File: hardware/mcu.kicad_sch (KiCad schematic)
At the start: 4 parts, among them U6 T113-S3

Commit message: 主晶片頁 C17~C19 footprint 由 DIP-24 改為 C_0603_1608Metric
複製元件時帶過去的錯誤封裝,check_power_rails.py 的 footprint 檢查抓到。
0.1uF ×2、2.2uF ×1 皆照 012 §4.1 用 0603。

Co-Authored-By: Claude Opus 5.5 <noreply@anthropic.com>
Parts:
- C17, C18, C19: footprint Package_DIP:DIP-24_W7.62mm -> Capacitor_SMD:C_0603_1608Metric
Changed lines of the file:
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@@
 			)
 		)
-		(property "Footprint" "Package_DIP:DIP-24_W7.62mm"
+		(property "Footprint" "Capacitor_SMD:C_0603_1608Metric"
 			(at 311.15 135.5852 0)
 			(hide yes)
@@
 			)
 		)
-		(property "Footprint" "Package_DIP:DIP-24_W7.62mm"
+		(property "Footprint" "Capacitor_SMD:C_0603_1608Metric"
 			(at 295.91 138.1252 0)
 			(hide yes)
@@
 			)
 		)
-		(property "Footprint" "Package_DIP:DIP-24_W7.62mm"
+		(property "Footprint" "Capacitor_SMD:C_0603_1608Metric"
 			(at 311.15 120.3452 0)
 			(hide yes)

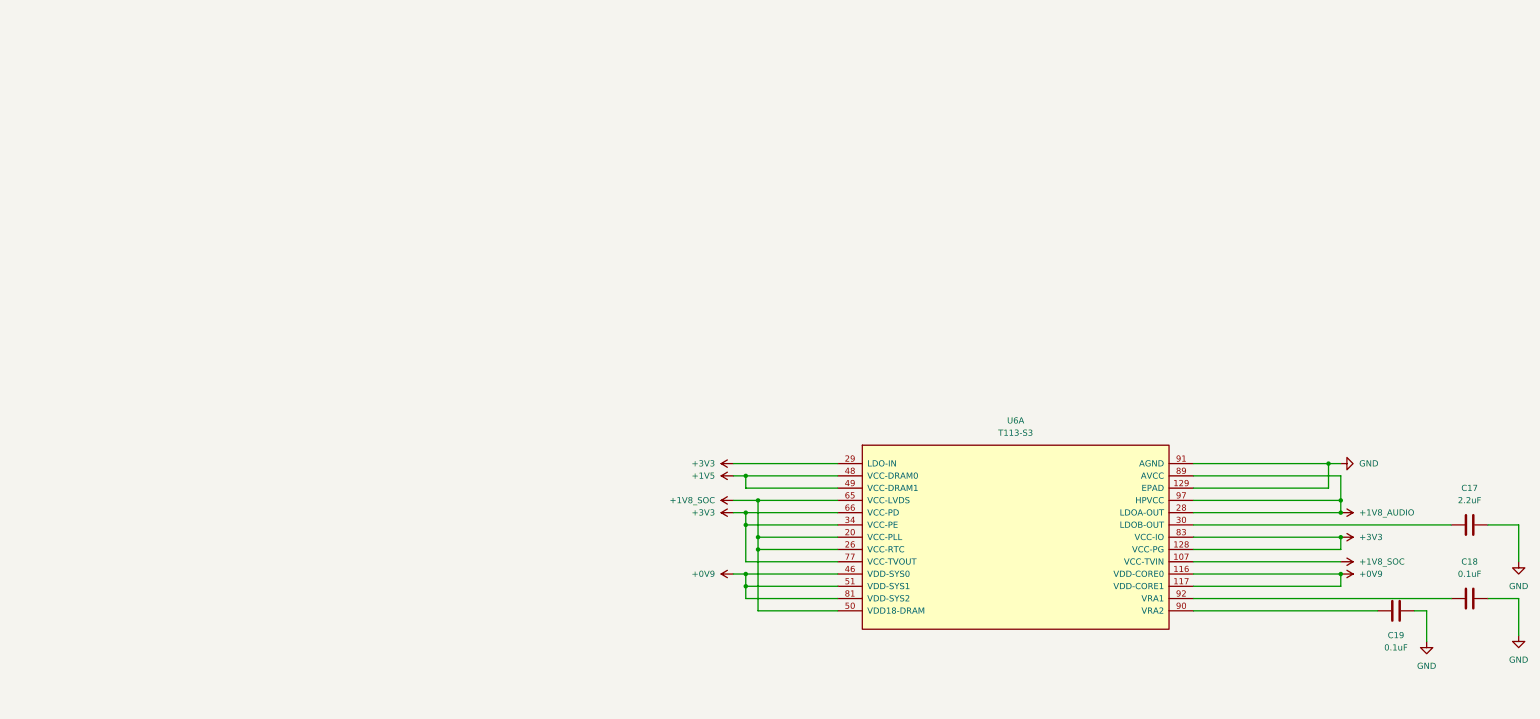
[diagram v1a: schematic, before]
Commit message: unit 2 的 12 腳接上全域標籤;修回被 KiCad 覆蓋的 footprint
unit 2（PB/PC/PF）先接 microSD 與 SPI NOR 這 12 腳:
  PF0~PF5 → SDC0_D1/D0/CLK/CMD/D3/D2
  PC2~PC7 → SPI0_CLK/CS0/MOSI/MISO/WP/HOLD
SDC0 的資料線編號不順(PF0=D1、PF1=D0、PF4=D3、PF5=D2),照 DS 抄,已核對無誤。
PF6 與 PB2~PB7 本輪不接。

★ C17~C19 的 footprint 被 KiCad 洗回 DIP-24:
  2413442 已經改成 C_0603 並 commit,但 KiCad 還開著舊的記憶體狀態,
  畫完 unit 2 存檔時整頁寫回去,把修正覆蓋掉。
  危險在於 git 只顯示「檔案被修改」,看不出是哪些修正被洗掉。
  → 012 新增 §6.2:git pull 之後、或任何人在檔案層改過 .kicad_sch 之後,
    一律關掉 KiCad 再重開。

check_power_rails.py 的跨頁白名單擴充 SDC0_* 與 SPI0_* 共 12 條,
附等待對象(儲存頁的 microSD 座 / SPI NOR)。

Co-Authored-By: Claude Opus 5 <noreply@anthropic.com>
Claude-Session: https://claude.ai/code/session_01HtGUWSQFey6W2g2grqgTMR
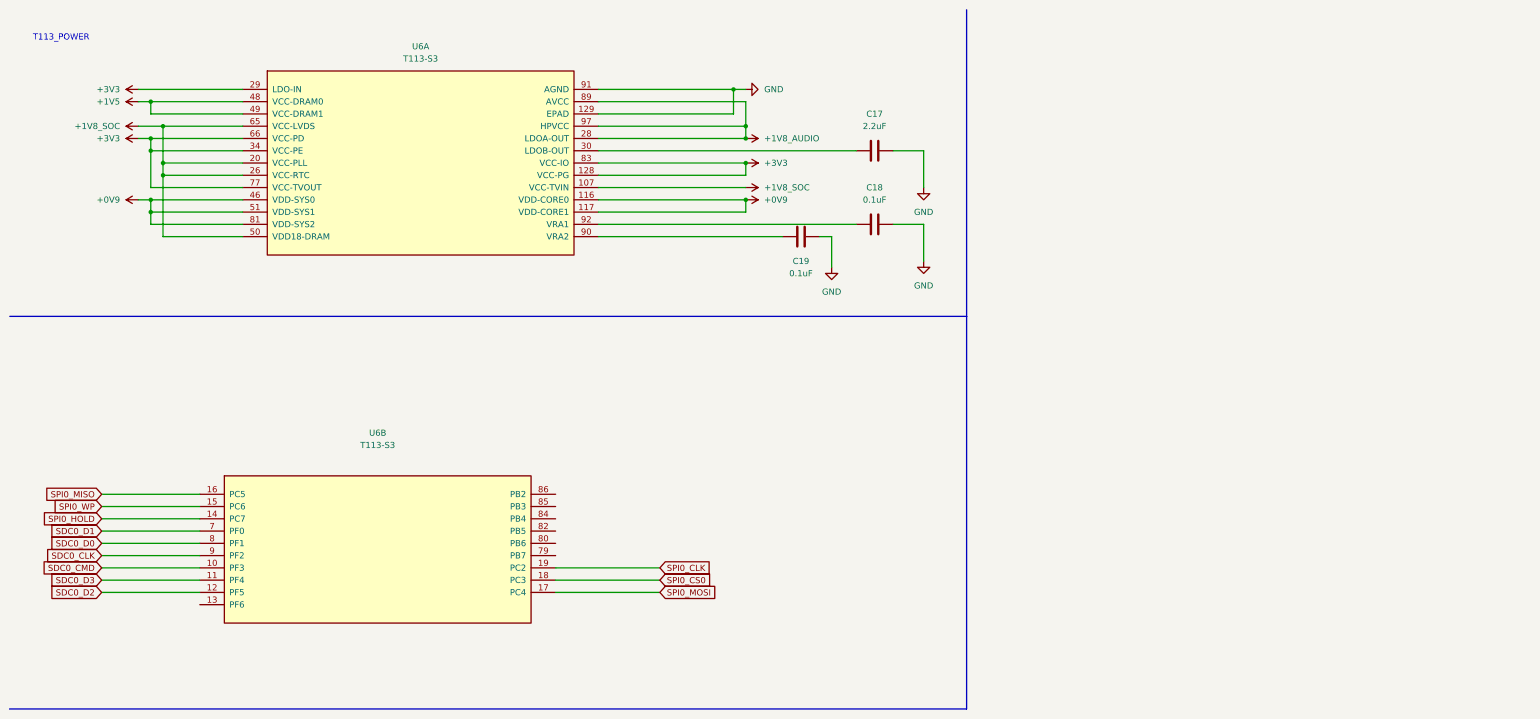
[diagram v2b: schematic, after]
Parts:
- added unit 2 of U6
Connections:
- new net SDC0_CLK: U6.9 (PF2)
- new net SDC0_CMD: U6.10 (PF3)
- new net SDC0_D0: U6.8 (PF1)
- new net SDC0_D1: U6.7 (PF0)
- new net SDC0_D2: U6.12 (PF5)
- new net SDC0_D3: U6.11 (PF4)
- new net SPI0_CLK: U6.19 (PC2)
- new net SPI0_CS0: U6.18 (PC3)
- new net SPI0_HOLD: U6.14 (PC7)
- new net SPI0_MISO: U6.16 (PC5)
- new net SPI0_MOSI: U6.17 (PC4)
- new net SPI0_WP: U6.15 (PC6)
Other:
- note added: "T113_POWER"
- moved on the sheet: C17, C18, C19, U6A

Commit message: ★ unit 2 完成(19/19):PB2~PB7 與 PF6 改為測試點
去處:
  SDC0 → microSD   PF0~PF5   全域標籤
  SPI0 → SPI NOR   PC2~PC7   全域標籤
  測試點            PB2~PB7   TP1~TP6
                   PF6       TP7
  皆用 TestPoint:TestPoint_Pad_D1.5mm,BOM 成本 $0(只是裸銅焊盤)

★ 推翻 007 §6.3 原本的「PB2~PB7 = I2S2 音訊 codec」規劃:
  查 Table 4-3 發現 I2S2 的 mux 有兩組(PB2~PB7 與 PF0/1/3/5/6),
  PF 那組已給 SDC0;但本板音訊是 T113 內建 codec(unit 6 的 AVCC/HPVCC/HPOUTL-R),
  根本不需要外接 I2S codec → 這 6 腳沒有用途。
  不拉排針的理由是 §4 規則①:PB 在 VCC-IO bank,
  那條軌掛著 microSD + SPI NOR + UART0 console,燒了就變無法診斷的磚。

⚠ SDC0 資料線編號不順(PF0=D1、PF1=D0、PF4=D3、PF5=D2),照 DS 抄已核對。

check_power_rails.py 跨頁白名單已含 SDC0_*/SPI0_* 共 12 條。

Co-Authored-By: Claude Opus 5 <noreply@anthropic.com>
Claude-Session: https://claude.ai/code/session_01HtGUWSQFey6W2g2grqgTMR
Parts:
- added TP1, TP2, TP3, TP4, TP5, TP6, TP7: TestPoint, TestPoint:TestPoint_Pad_D1.5mm, symbol Connector:TestPoint
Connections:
- net at U6.13 (PF6): now also TP7.1
- net at U6.79 (PB7): now also TP6.1
- net at U6.80 (PB6): now also TP5.1
- net at U6.82 (PB5): now also TP4.1
- net at U6.84 (PB4): now also TP3.1
- net at U6.85 (PB3): now also TP2.1
- net at U6.86 (PB2): now also TP1.1

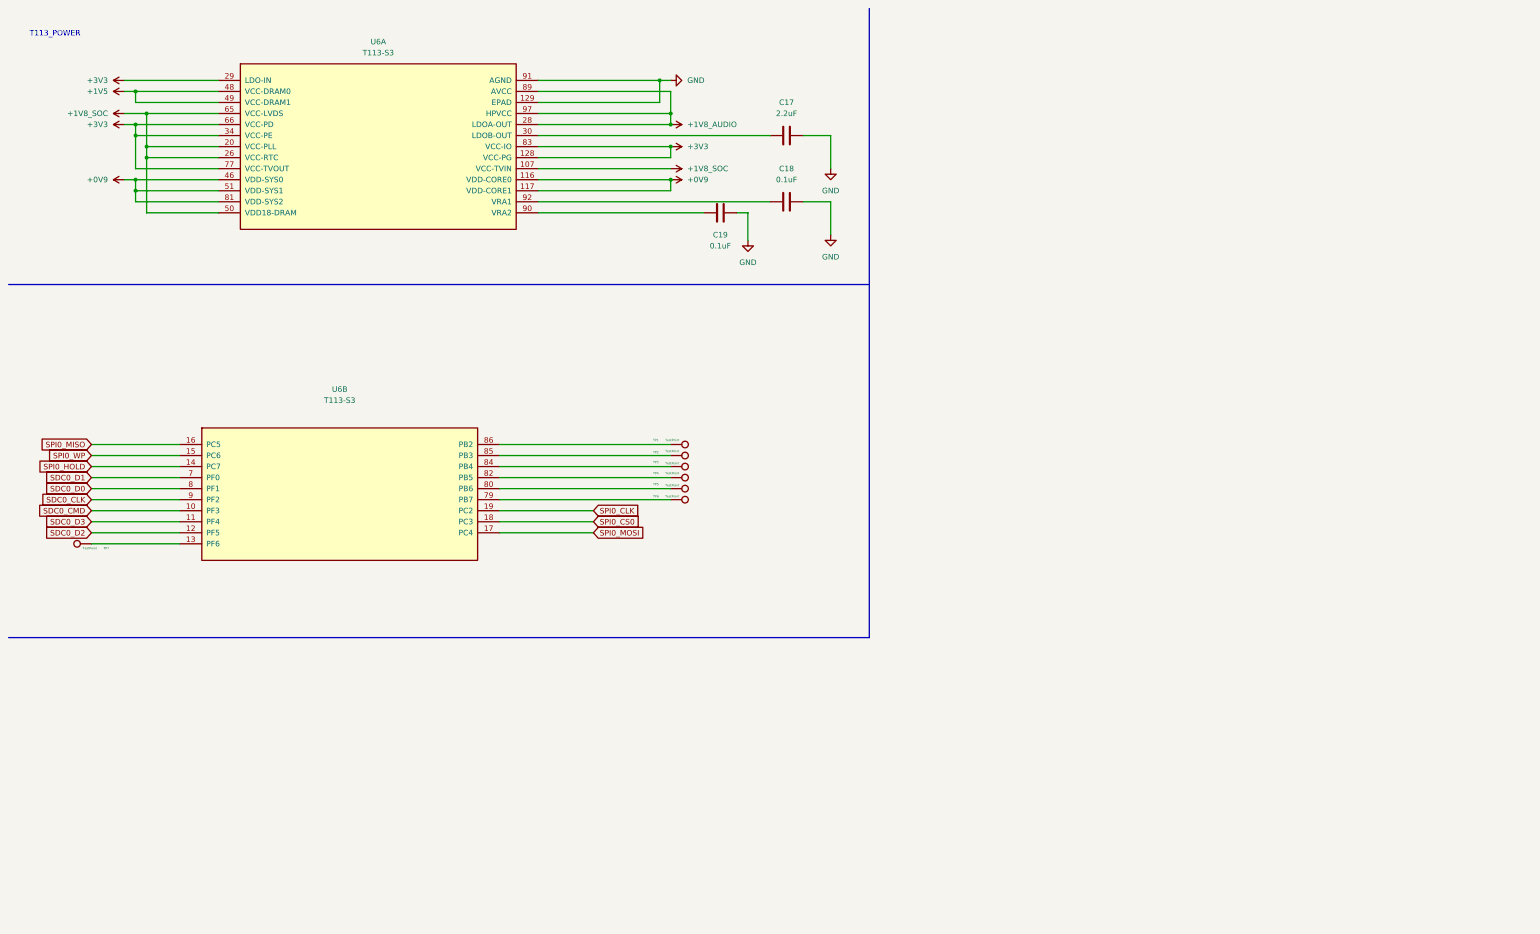
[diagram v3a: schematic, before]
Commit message: ★ unit 3 完成(23/23):MIPI 直通 + 0Ω 分支到 RGB
PD0~PD9    一分為二:MIPI 標籤直通、再經 R10~R19(0R) 分支到 RGB 標籤
PD10~PD21  直接接 LCD0_D14/D15/D18~D23/CLK/DE/HSYNC/VSYNC
PD22       測試點 TP8

0Ω 不在 MIPI 路徑上而在分支上,所以不違反「MIPI 不能加串聯電阻」。
跑 MIPI 時 0Ω 不焊,ADV7511 完全脫離主幹(概念 ⑤)。

三個照 DS 抄、不能推的地方(已逐行對 Table 4-3 核):
  LCD0-D 跳號①  PD5=D7 → PD6=D10
  LCD0-D 跳號②  PD11=D15 → PD12=D18(D16/D17 在 PB6/PB7,已放棄 → RGB666 的由來)
  pin 號順序反   PD12=pin70、PD13=pin69
這種地方推錯了 netlist 也看不出來 —— 名字都是合法的 LCD0_Dxx。

check_power_rails.py 跨頁白名單補 DSI_* 10 條 + LCD0_* 22 條。
R10~R19 與 TP8 的 footprint 一併填上。

★ 自我檢討:012 §6.2 剛寫完「KiCad 開著時不要在檔案層改 .kicad_sch」,
下一個動作就違反了 —— 偵測到 KiCad 開著只印了警告就繼續執行。
教訓:警告訊息不是防護措施,要擋就要硬性中止。

Co-Authored-By: Claude Opus 5 <noreply@anthropic.com>
Claude-Session: https://claude.ai/code/session_01HtGUWSQFey6W2g2grqgTMR
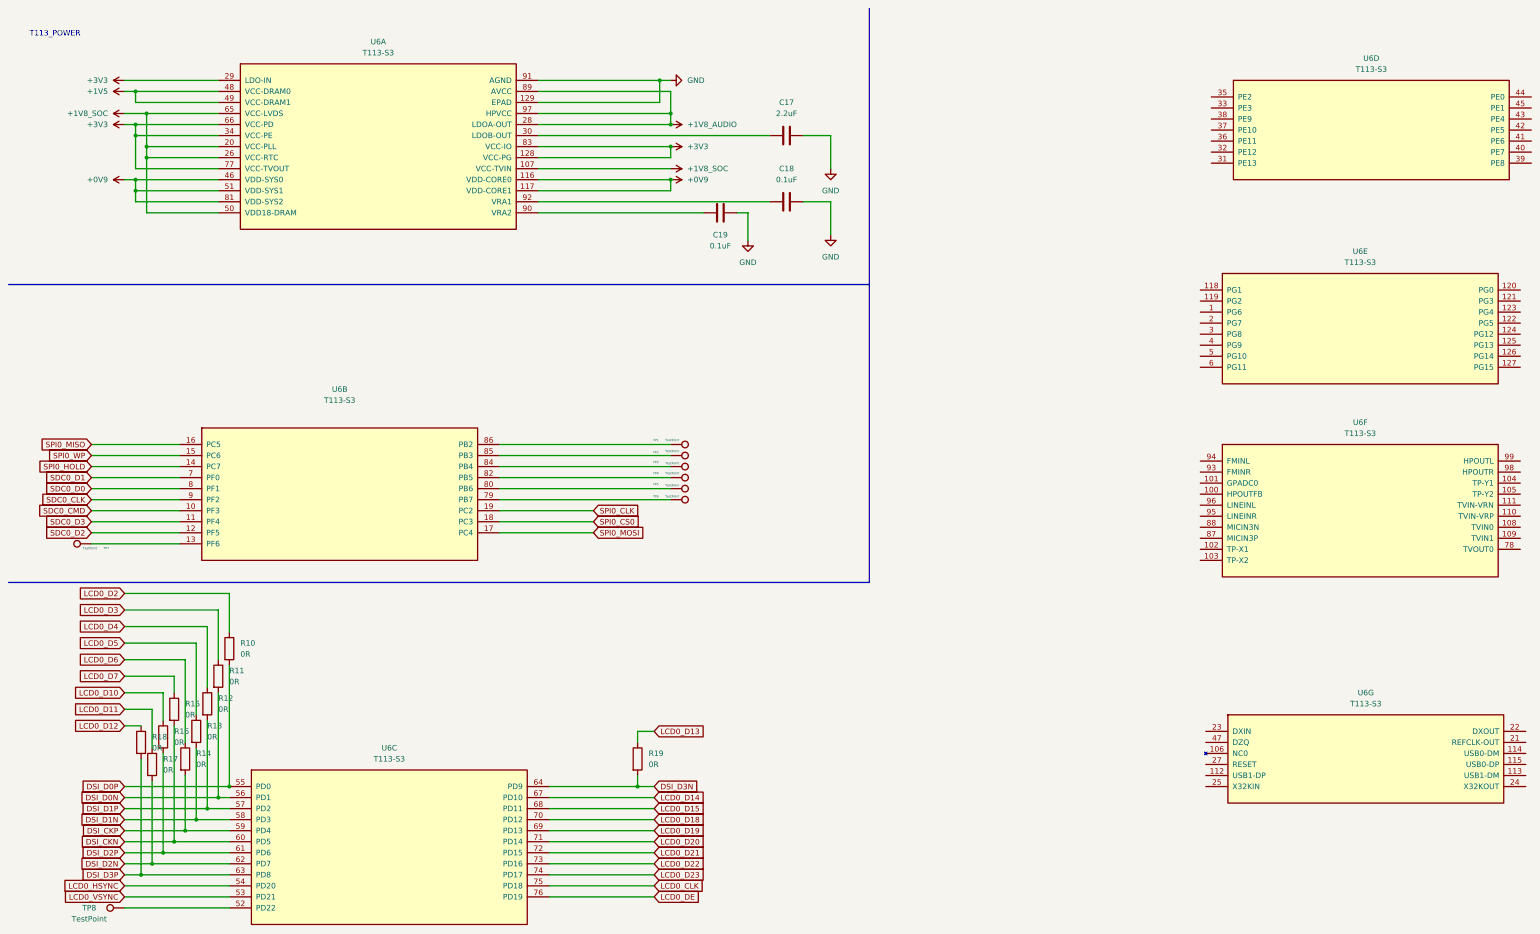
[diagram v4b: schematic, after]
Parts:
- added R10, R11, R12, R13, R14, R15, R16, R17, R18, R19: 0R, Resistor_SMD:R_0603_1608Metric, symbol Device:R
- added TP8: TestPoint, TestPoint:TestPoint_Pad_D1.5mm, symbol Connector:TestPoint
- added unit 5 of U6
- added unit 6 of U6
- added unit 7 of U6
- added unit 4 of U6
- added unit 3 of U6
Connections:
- new net: TP8.1, U6.52 (PD22)
- new net DSI_CKN: R15.2, U6.60 (PD5)
- new net DSI_CKP: R14.2, U6.59 (PD4)
- new net DSI_D0N: R11.2, U6.56 (PD1)
- new net DSI_D0P: R10.2, U6.55 (PD0)
- new net DSI_D1N: R13.2, U6.58 (PD3)
- new net DSI_D1P: R12.2, U6.57 (PD2)
- new net DSI_D2N: R17.2, U6.62 (PD7)
- new net DSI_D2P: R16.2, U6.61 (PD6)
- new net DSI_D3N: R19.2, U6.64 (PD9)
- new net DSI_D3P: R18.2, U6.63 (PD8)
- new net LCD0_CLK: U6.75 (PD18)
- new net LCD0_D10: R16.1
- new net LCD0_D11: R17.1
- new net LCD0_D12: R18.1
- new net LCD0_D13: R19.1
- new net LCD0_D14: U6.67 (PD10)
- new net LCD0_D15: U6.68 (PD11)
- new net LCD0_D18: U6.70 (PD12)
- new net LCD0_D19: U6.69 (PD13)
- new net LCD0_D2: R10.1
- new net LCD0_D20: U6.71 (PD14)
- new net LCD0_D21: U6.72 (PD15)
- new net LCD0_D22: U6.73 (PD16)
- new net LCD0_D23: U6.74 (PD17)
- new net LCD0_D3: R11.1
- new net LCD0_D4: R12.1
- new net LCD0_D5: R13.1
- new net LCD0_D6: R14.1
- new net LCD0_D7: R15.1
- new net LCD0_DE: U6.76 (PD19)
- new net LCD0_HSYNC: U6.54 (PD20)
- new net LCD0_VSYNC: U6.53 (PD21)

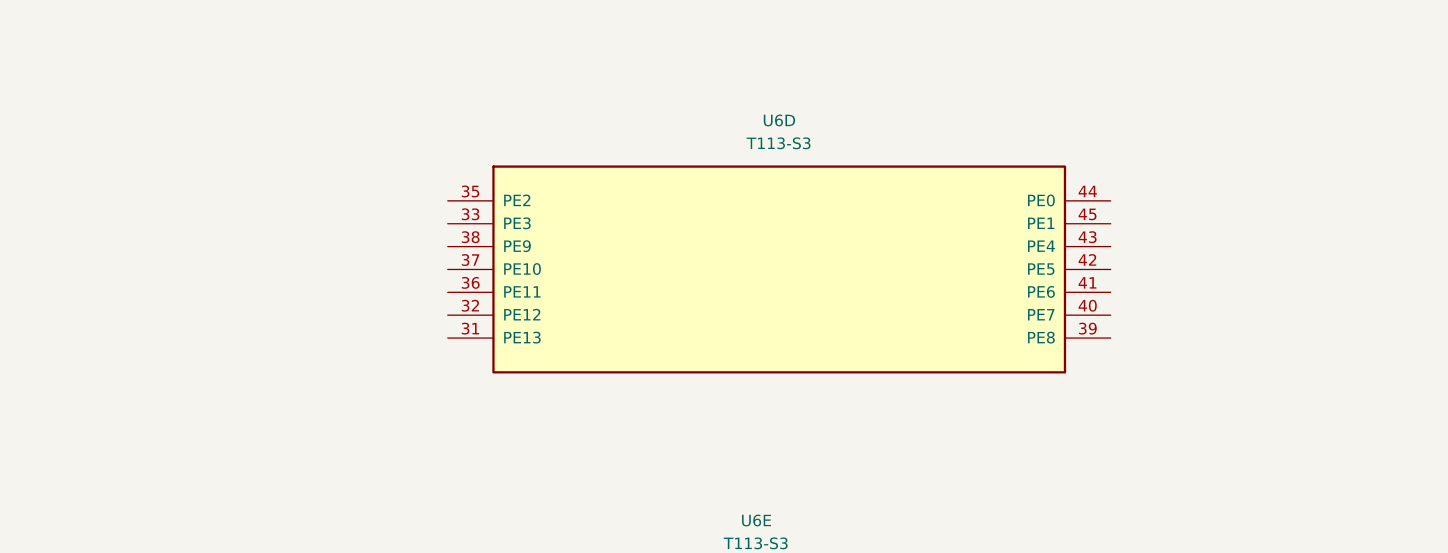
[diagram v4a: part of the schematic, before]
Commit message: ★ unit 4 完成(14/14):PE bank 網路;三處與原規劃不同
PE0~PE9   RMII 十條訊號(CRS_DV/RXD0/RXD1/REF_CLK/TXD0/TXD1/TX_EN/RXER/MDC/MDIO)
PE10      測試點 TP9
PE11      PHY_RESET_N
PE12/13   測試點 TP10/TP11

三處更正(對 DS Table 4-3 逐行核):
① PE7 存在且是 RMII-RXER —— 原規劃漏了這支,是 RMII 標準訊號之一
② PE10 的 mux 沒有 PHY RESET
   實際是 NCSI0-D6|UART1-TX|PWM4|IR-RX|JTAG-DO|EPHY-25M
   007 原寫「EPHY-25M(或 PHY RESET)」是推測,datasheet 不支持
   → PHY_RESET_N 改放 PE11,PE10 改測試點(兩種時脈架構都保留彈性)
③ PE9 的標籤一度打成 RMII_MDI0(數字零)而非 RMII_MDIO(字母 O)
   第五次命名坑,也是最難目視發現的一種

⚠ PE3 的 DS 名稱是 RMII-TXCK 不是 RMII-REF-CLK,標籤暫用後者。
  要查 EMAC 章節確認這支是輸入還是輸出 ——
  RMII 的 REF_CLK 有「MAC 提供」與「PHY 提供」兩種架構,決定 PHY 要不要自帶晶振。

PHY_RESET_N 放 PE(與 RMII 同 bank)不違反 §4 規則③:
那條規則防的是「一個 bank 燒掉害好幾個介面失效」,
PE 燒掉時 RMII 資料線本來就死了;真正該打散的是不同介面的控制訊號。

U6 進度:82 / 129 腳。測試點 TP1~TP11 連續無跳號。

Co-Authored-By: Claude Opus 5 <noreply@anthropic.com>
Claude-Session: https://claude.ai/code/session_01HtGUWSQFey6W2g2grqgTMR
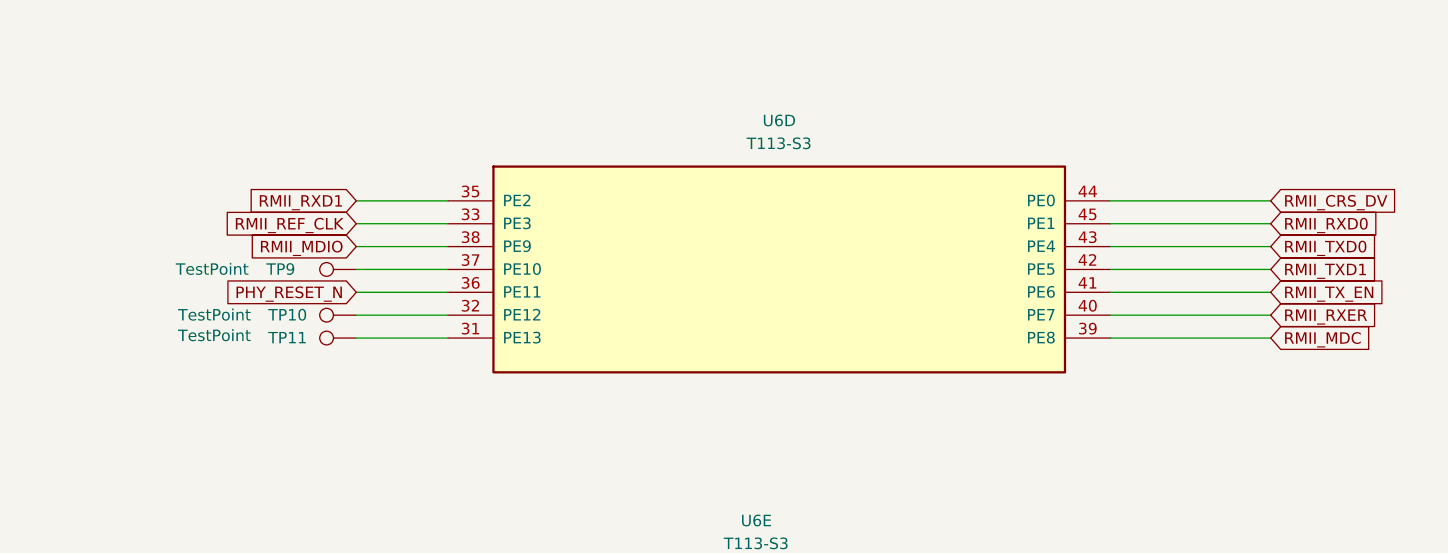
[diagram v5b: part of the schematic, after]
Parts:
- added TP10, TP11, TP9: TestPoint, Relay_THT:Relay_DPDT_Schrack-RT2-FormC_RM5mm, symbol Connector:TestPoint
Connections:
- net at U6.31 (PE13): now also TP11.1
- net at U6.32 (PE12): now also TP10.1
- net RMII_REF_CLK: now reaches U6.33 (PE3)
- net RMII_RXD1: now reaches U6.35 (PE2)
- net PHY_RESET_N: now reaches U6.36 (PE11)
- net at U6.37 (PE10): now also TP9.1
- net RMII_MDIO: now reaches U6.38 (PE9)
- net RMII_MDC: now reaches U6.39 (PE8)
- net RMII_RXER: now reaches U6.40 (PE7)
- net RMII_TX_EN: now reaches U6.41 (PE6)
- net RMII_TXD1: now reaches U6.42 (PE5)
- net RMII_TXD0: now reaches U6.43 (PE4)
- net RMII_CRS_DV: now reaches U6.44 (PE0)
- net RMII_RXD0: now reaches U6.45 (PE1)
